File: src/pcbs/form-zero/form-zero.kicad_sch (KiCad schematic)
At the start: 124 parts, among them J1 Conn_01x17_Pin, SW1 SW_Push, SW10 SW_Push, SW11 SW_Push, SW12 SW_Push, SW13 SW_Push, SW14 SW_Push, SW15 SW_Push, SW16 SW_Push, SW17 SW_Push, SW18 SW_Push, SW19 SW_Push, SW2 SW_Push, SW20 SW_Push, SW21 SW_Push, SW22 SW_Push, SW23 SW_Push, SW24 SW_Push, SW25 SW_Push, SW26 SW_Push, SW27 SW_Push, SW28 SW_Push, SW29 SW_Push, SW3 SW_Push, SW30 SW_Push, SW31 SW_Push, SW32 SW_Push, SW33 SW_Push, SW34 SW_Push, SW35 SW_Push, SW36 SW_Push, SW37 SW_Push, SW38 SW_Push, SW39 SW_Push, SW4 SW_Push, SW40 SW_Push, SW41 SW_Push, SW42 SW_Push, SW43 SW_Push, SW44 SW_Push, SW45 SW_Push, SW46 SW_Push, SW47 SW_Push, SW48 SW_Push, SW49 SW_Push, SW5 SW_Push, SW50 SW_Push, SW51 SW_Push, SW52 SW_Push, SW53 SW_Push, SW54 SW_Push, SW55 SW_Push, SW56 SW_Push, SW57 SW_Push, SW58 SW_Push, SW59 SW_Push, SW6 SW_Push, SW60 SW_Push, SW61 SW_Push, SW7 SW_Push, SW8 SW_Push, SW9 SW_Push

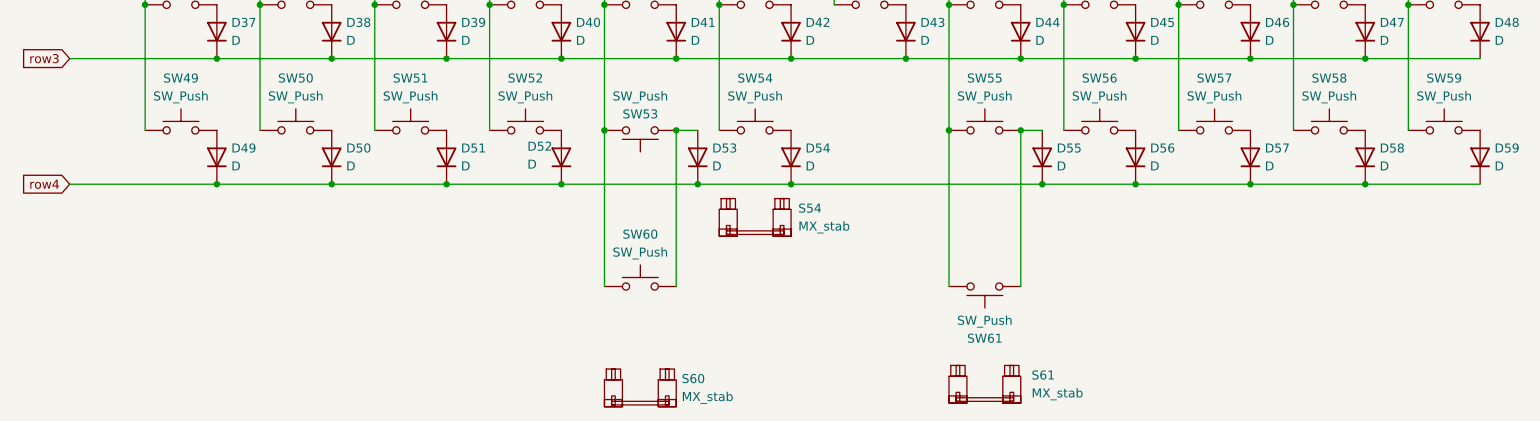
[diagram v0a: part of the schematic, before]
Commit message: add bottom row: 1.25, 1.25, 7, 1.25, 1.25
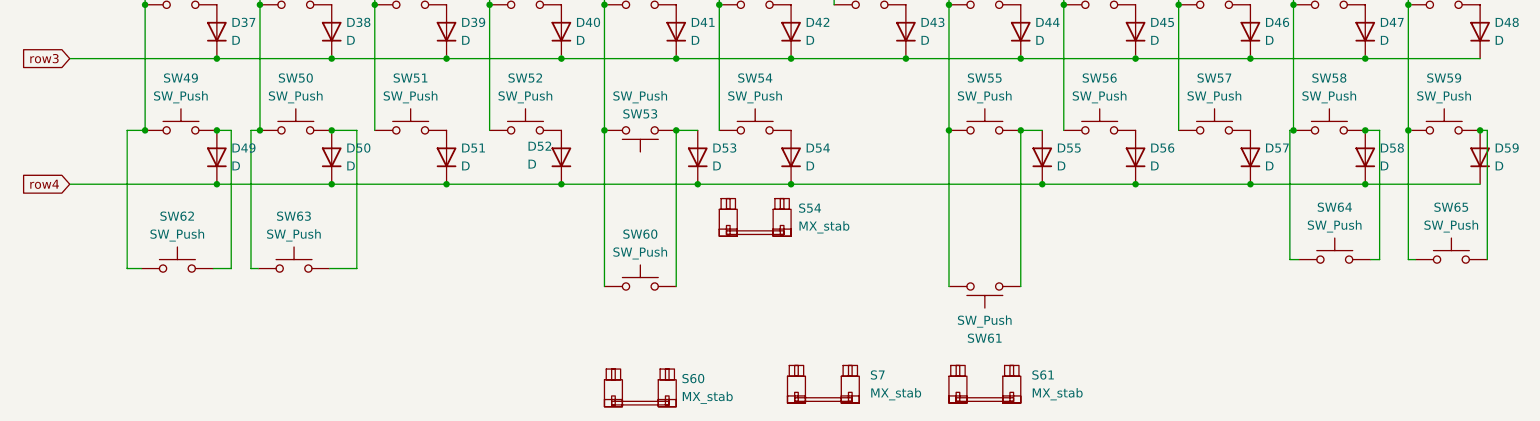
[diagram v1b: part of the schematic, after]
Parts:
- added S7: MX_stab, PCM_marbastlib-mx:STAB_MX_7u, symbol marbastlib-mx:MX_stab
- added SW62, SW63, SW64, SW65: SW_Push, PCM_marbastlib-mx:SW_MX_HS_CPG151101S11_1.25u, symbol Switch:SW_Push
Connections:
- net col0: now also SW62.1
- net col1: now also SW63.1
- net col10: now also SW64.1
- net col11: now also SW65.1
- net at D58.2 (A), SW58.2: now also SW64.2
- net at D59.2 (A), SW59.2: now also SW65.2
- net at D49.2 (A), SW49.2: now also SW62.2
- net at D50.2 (A), SW50.2: now also SW63.2
